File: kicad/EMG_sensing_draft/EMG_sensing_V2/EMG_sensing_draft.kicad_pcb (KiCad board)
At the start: 2 copper layers, 49.4 x 60.1 mm, 157 parts, among them J1 USB_A_0480370001, J2 Conn_01x09, J3 DEBUG, U1 MCP6N11-002E/SN, U10 RP2040, U11 RN4871-I/RM140, U12 MCP1702T-3302E_CB, U13 Opamp_MCP6024T-E/ST, U14 Opamp_MCP6024T-E/ST, U15 Opamp_MCP6024T-E/ST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

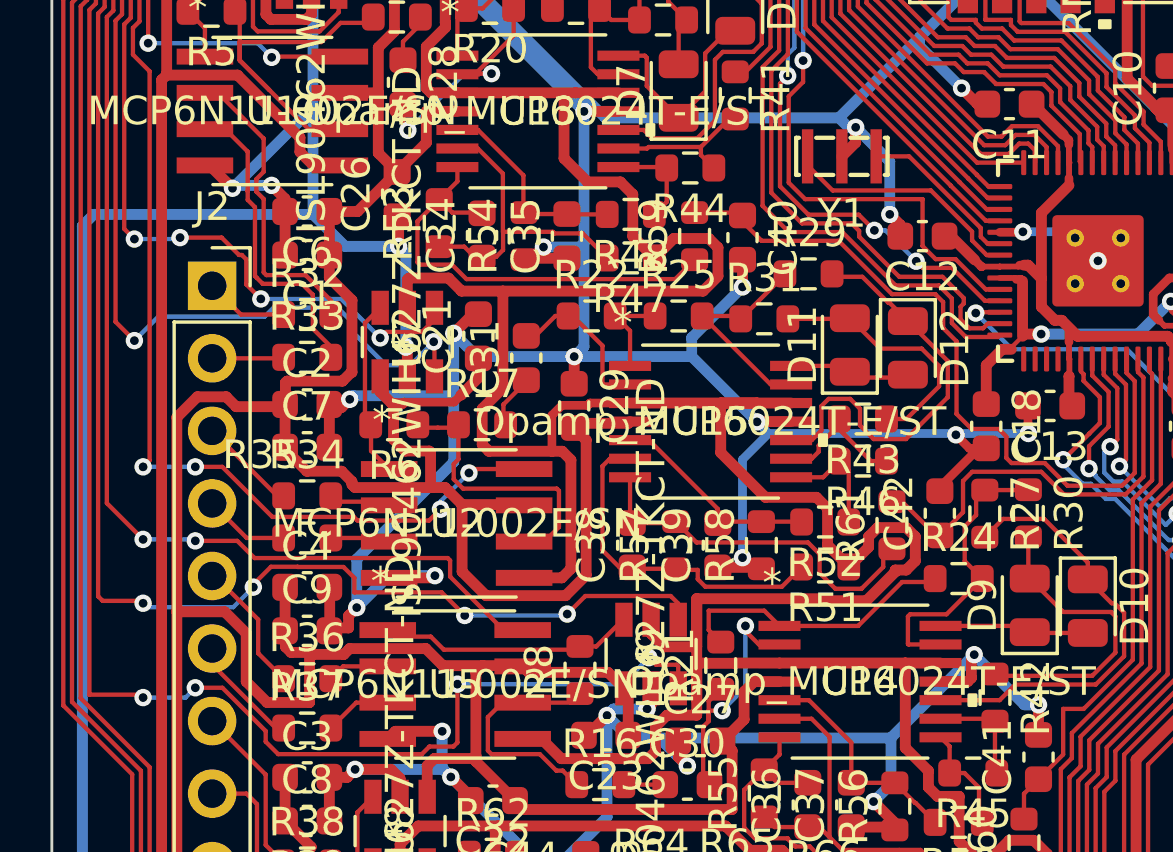
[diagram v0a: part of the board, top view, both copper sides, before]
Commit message: Fix errors in layout
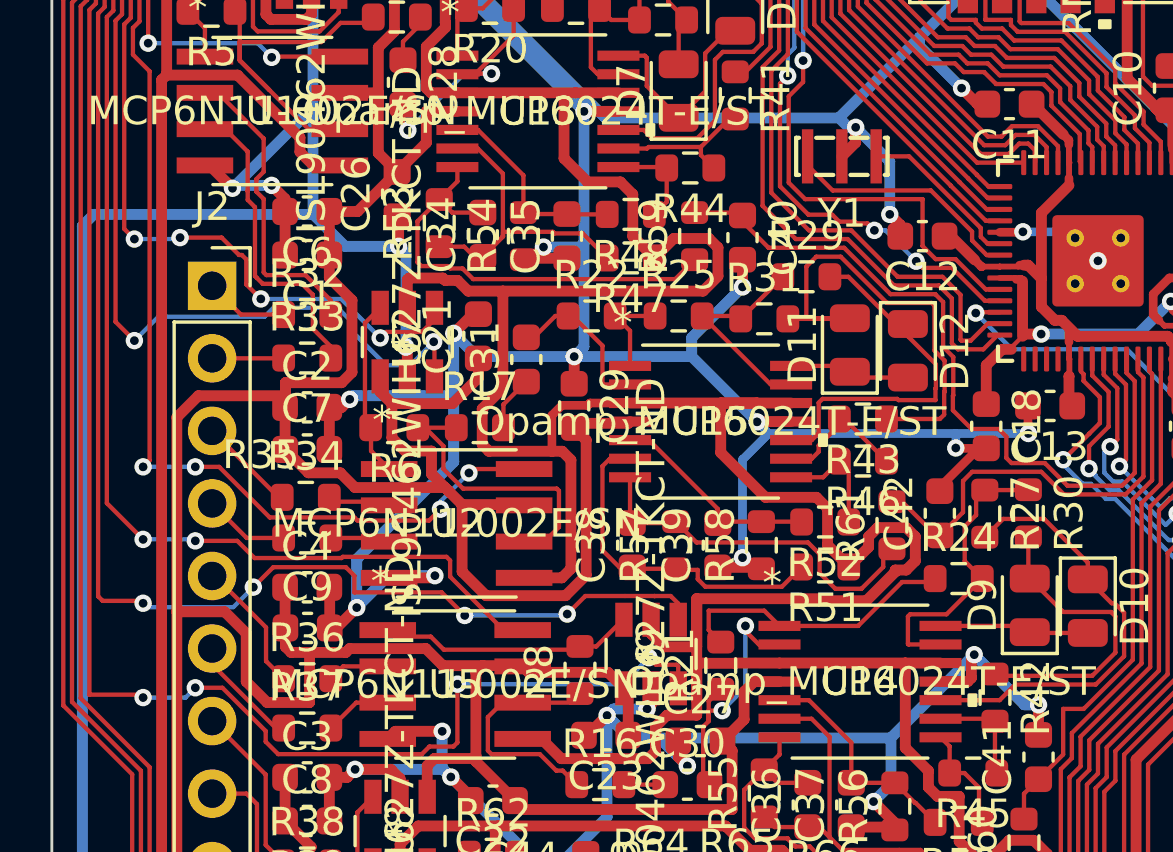
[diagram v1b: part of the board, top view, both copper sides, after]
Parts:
- moved R17 0.13 mm to (237.8, 52.3)
- moved R29 0.13 mm to (249.3, 47.0)
- moved C9 0.10 mm to (231.8, 59.3)
- moved C2 0.10 mm to (231.8, 51.6)
- moved D12 0.10 mm to (252.8, 49.6)
- moved R6 0.10 mm to (234.8, 52.3)
- moved C7 0.08 mm to (231.8, 53.1)
- moved R34 0.07 mm to (231.7, 54.8)
- moved C31 0.05 mm to (239.5, 49.9)
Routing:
- net Net-(D11-Pad2): track 9.03 -> 16.9 mm
- net Net-(D12-Pad1): track 14.7 -> 12.8 mm
- net /POT_CHANGE_ONE: track 42.4 -> 43.2 mm
- net /V_DIFF_TWO: track 9.67 -> 10.4 mm
- net /POT_CS_ONE: track 45.4 -> 46.0 mm

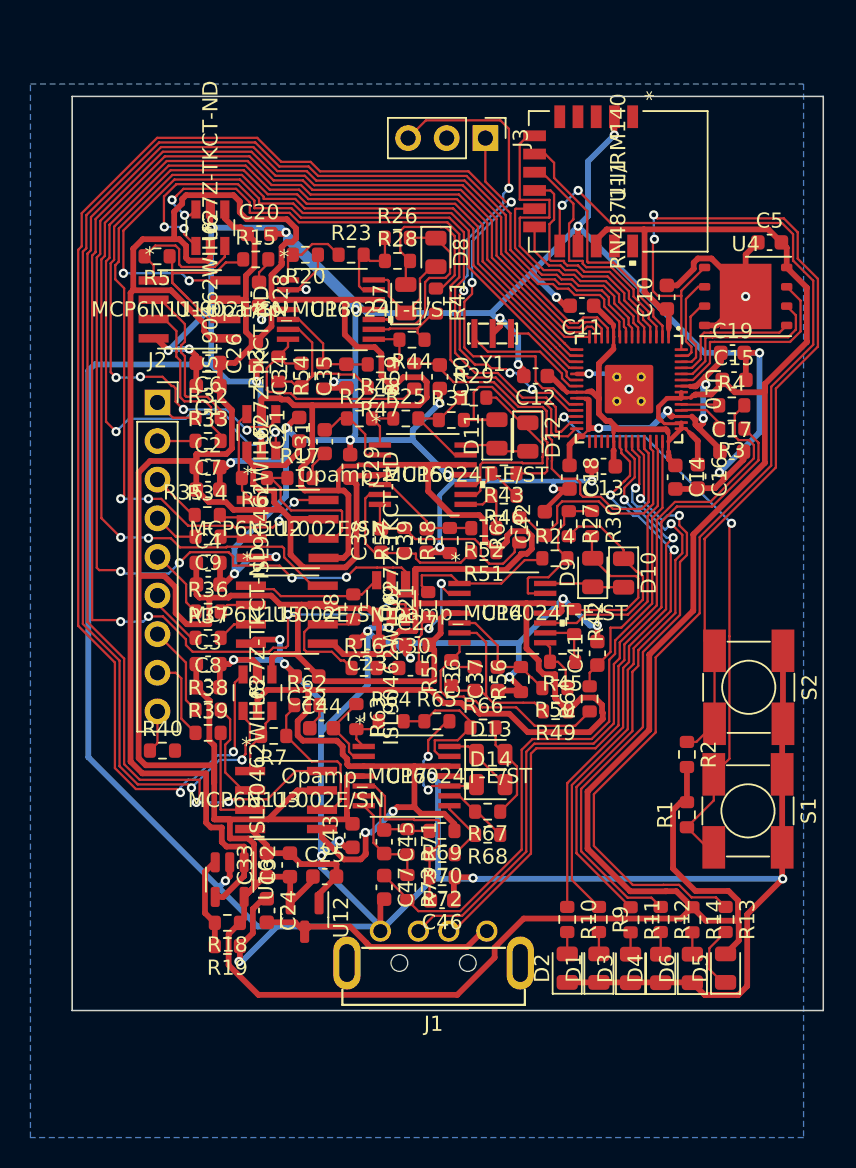
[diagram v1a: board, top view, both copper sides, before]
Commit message: removed references from silkscreen
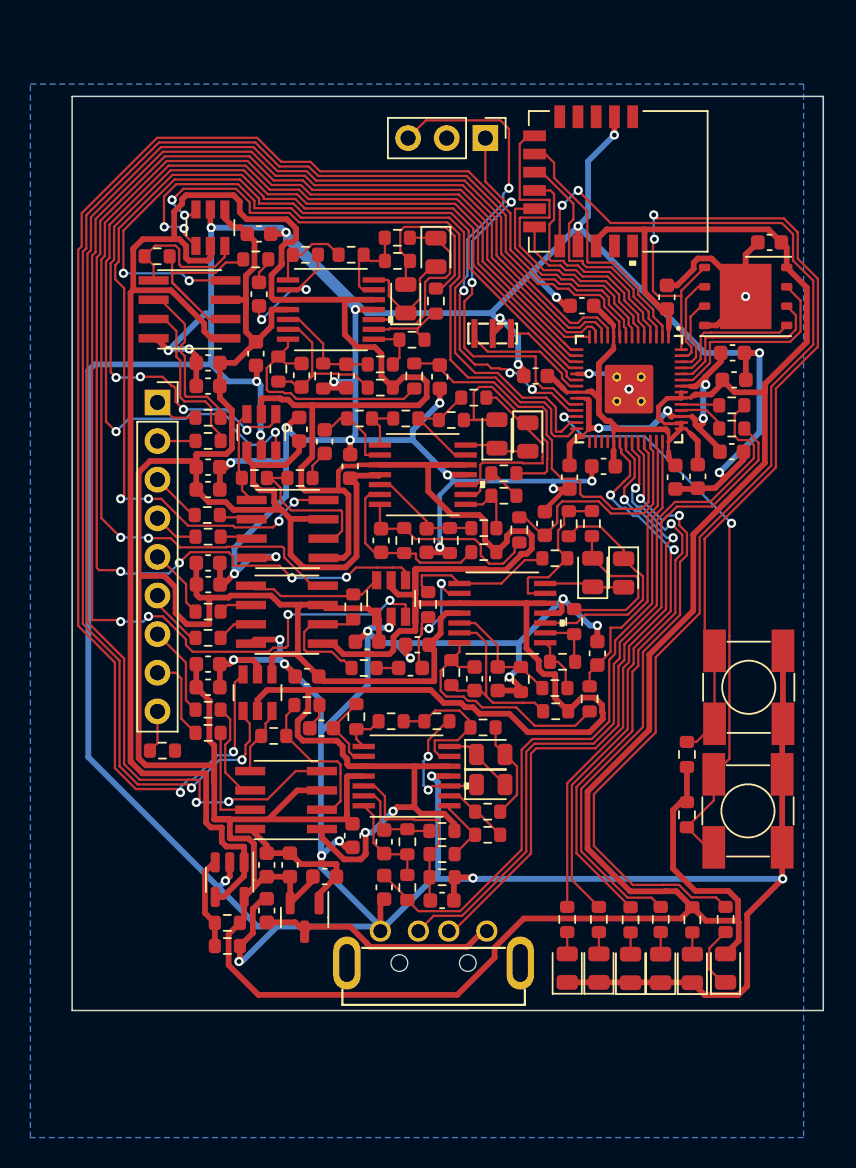
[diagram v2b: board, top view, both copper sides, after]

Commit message: fixed rn4871 position
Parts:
- moved U11 4.01 mm to (259.2, 28.8), turned to 0 degrees
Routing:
- net GND: track 449.5 -> 139.8 mm
- net /RX_IND: track 23.0 -> 10.7 mm
- net Net-(R2-Pad1): track 61.6 -> 71.6 mm, vias 2 -> 0
- net +3.3V: track 357.7 -> 348.2 mm
- net Net-(R13-Pad1): track 76.6 -> 67.7 mm, vias 2 -> 0
- net /BLE_TX: track 16.2 -> 9.84 mm
- net /POT_CS_THREE: track 87.2 -> 91.7 mm
- net Net-(R12-Pad1): track 39.2 -> 35.0 mm
- net /RST_N: track 14.8 -> 18.7 mm
- net /BLE_RX: track 16.9 -> 13.3 mm
- net /RTS: track 15.5 -> 16.3 mm
- net /CTS: track 12.1 -> 12.4 mm, vias 0 -> 2

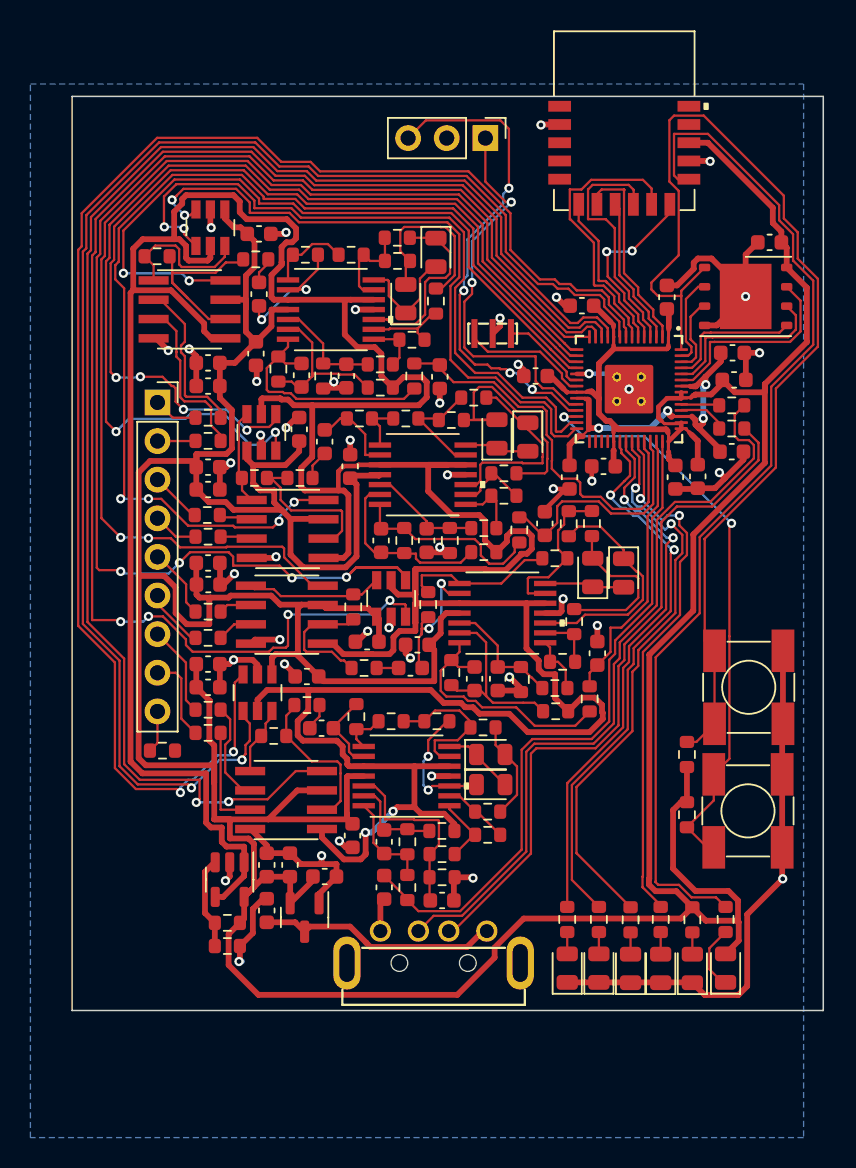
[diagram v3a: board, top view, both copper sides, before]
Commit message: added two layers to board
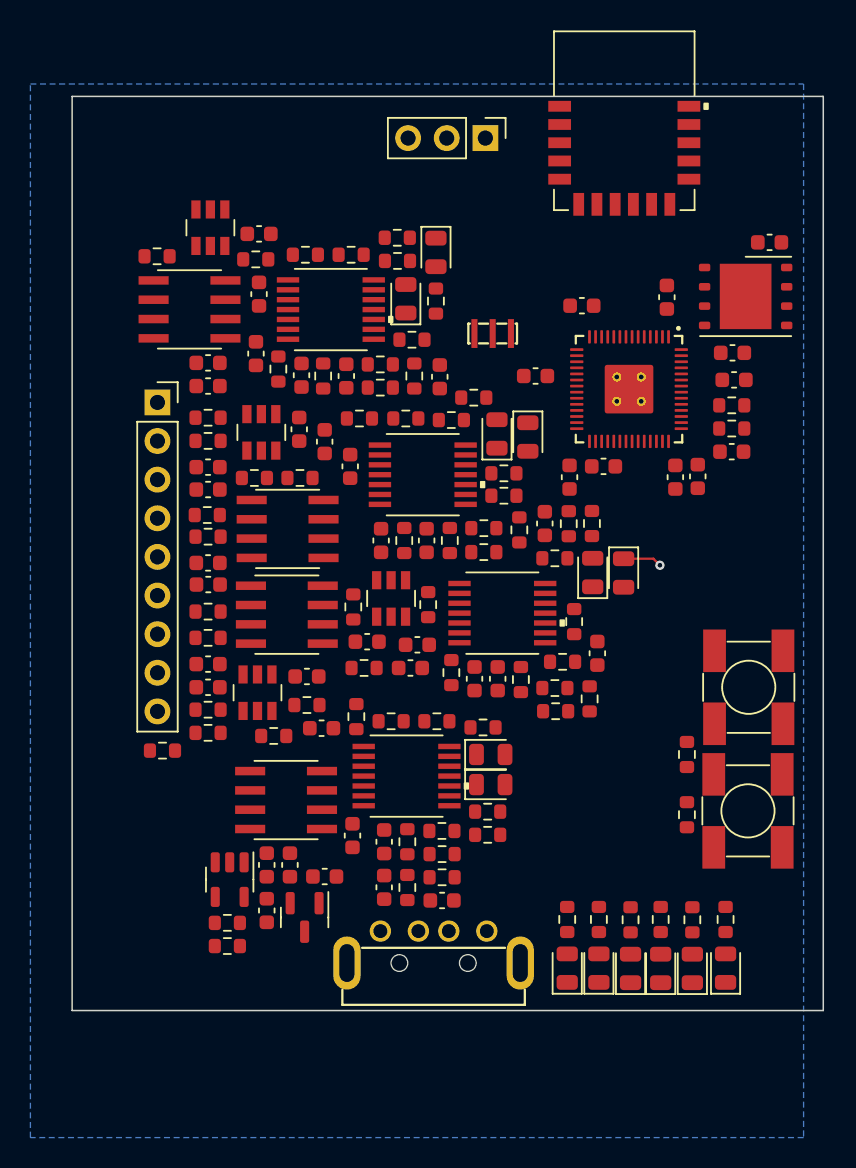
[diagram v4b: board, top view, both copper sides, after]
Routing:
- net +3.3V: track 348.2 -> 0.00 mm
- net +1.65V: track 253.1 -> 0.00 mm, vias 2 -> 0
- net GND: track 139.8 -> 0.00 mm, vias 44 -> 0
- net /POT_CHANGE_FOUR: track 98.3 -> 0.00 mm, vias 2 -> 0
- net /DIF_AMP_FOUR_CAL: track 96.3 -> 0.00 mm, vias 2 -> 0
- net /POT_CS_FOUR: track 95.0 -> 0.00 mm, vias 2 -> 0
- net /POT_CHANGE_THREE: track 94.3 -> 0.00 mm, vias 4 -> 0
- net /POT_CS_THREE: track 91.7 -> 0.00 mm, vias 4 -> 0
- net /DIF_AMP_THREE_CAL: track 76.0 -> 0.00 mm, vias 2 -> 0
- net Net-(R2-Pad1): track 71.6 -> 0.00 mm
- net /DIF_AMP_TWO_CAL: track 71.4 -> 0.00 mm, vias 4 -> 0
- net Net-(R13-Pad1): track 67.7 -> 0.00 mm
- net /POT_CHANGE_TWO: track 66.3 -> 0.00 mm, vias 2 -> 0
- net /POT_CS_TWO: track 61.8 -> 0.00 mm, vias 4 -> 0
- net /USB_D+: track 49.6 -> 0.00 mm
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- added copper zone on In1.Cu, net GND
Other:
- copper layers 2 -> 4

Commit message: fixed overlapping courtyards
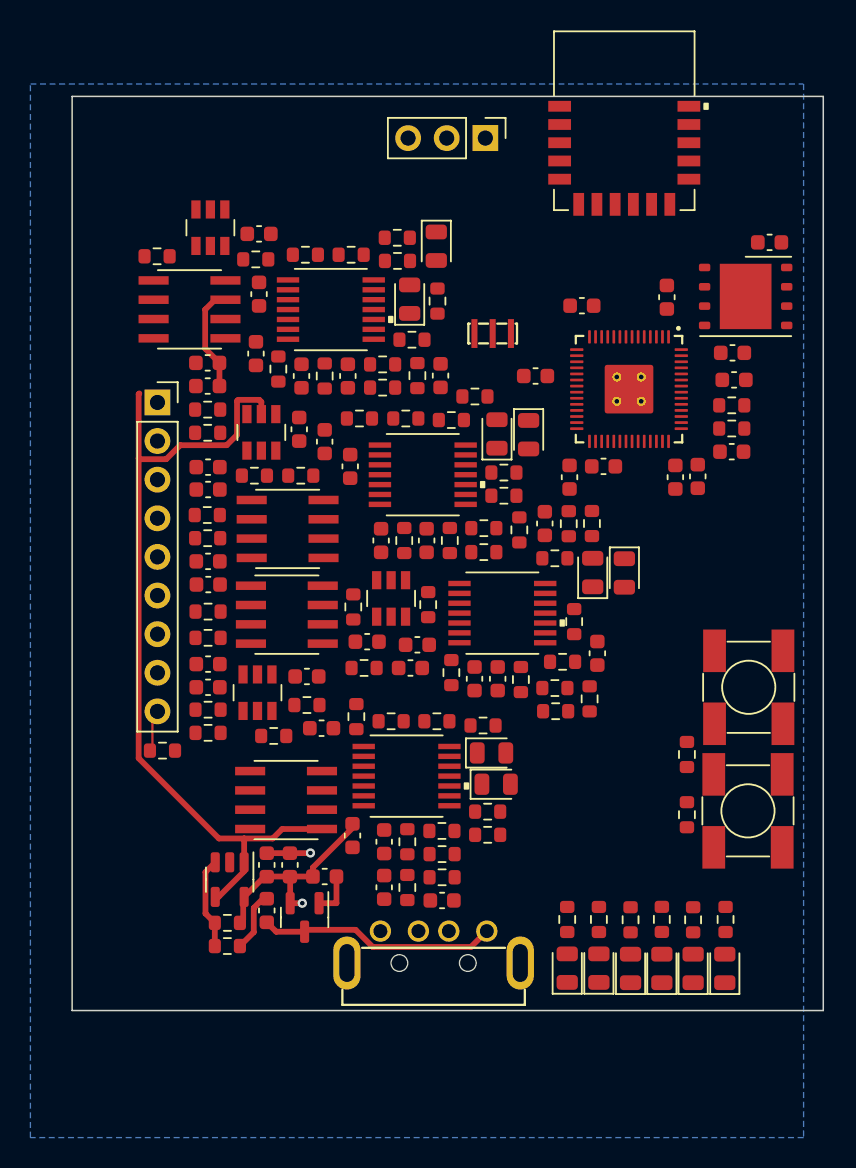
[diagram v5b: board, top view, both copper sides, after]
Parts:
- moved R32 0.53 mm to (231.8, 47.8)
- moved R33 0.53 mm to (231.8, 49.4)
- moved D8 0.41 mm to (246.8, 37.1)
- moved D14 0.36 mm to (250.7, 72.5)
- moved D7 0.26 mm to (245.1, 40.6)
- moved R59 0.20 mm to (245.6, 45.6)
- moved R17 0.16 mm to (237.9, 52.2)
- moved D12 0.16 mm to (252.9, 49.5)
- moved R47 0.15 mm to (243.3, 46.4)
- moved R48 0.15 mm to (243.3, 44.9)
- moved R6 0.15 mm to (234.8, 52.2)
- moved R66 0.13 mm to (249.9, 68.6)
- moved D13 0.11 mm to (250.4, 70.4)
- moved R29 0.11 mm to (249.4, 47.0)
- moved R35 0.10 mm to (231.8, 56.3)
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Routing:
- net +1.65V: track 0.00 -> 55.1 mm
- net +3.3V: track 0.00 -> 21.0 mm, vias 0 -> 1
- net Net-(C24-Pad2): track 0.00 -> 15.7 mm
- net GND: track 0.00 -> 9.76 mm, vias 0 -> 1
- net Net-(R18-Pad2): track 0.00 -> 6.03 mm
- net Net-(J2-Pad9): track 0.00 -> 2.79 mm
- net Net-(D10-Pad1): track 2.57 -> 0.00 mm, vias 1 -> 0
- added copper zone on In2.Cu, net +3.3V
